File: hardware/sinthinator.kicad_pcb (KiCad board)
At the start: 2 copper layers, 100.9 x 144.5 mm, 56 parts, among them J1 3.5mm TRRS, J2 USB-C, M2 MountingHole_2.2mm_M2, SW1 SW_Push, SW2 SW_Push, SW3 SW_Push, U1 CAP1206, U2 PCA9544APW, U3 MCP4725, U4 CAP1206, U5 CAP1206, U7 AMS1117-3.3, U8 PAM8302A, U9 STM32C011F6

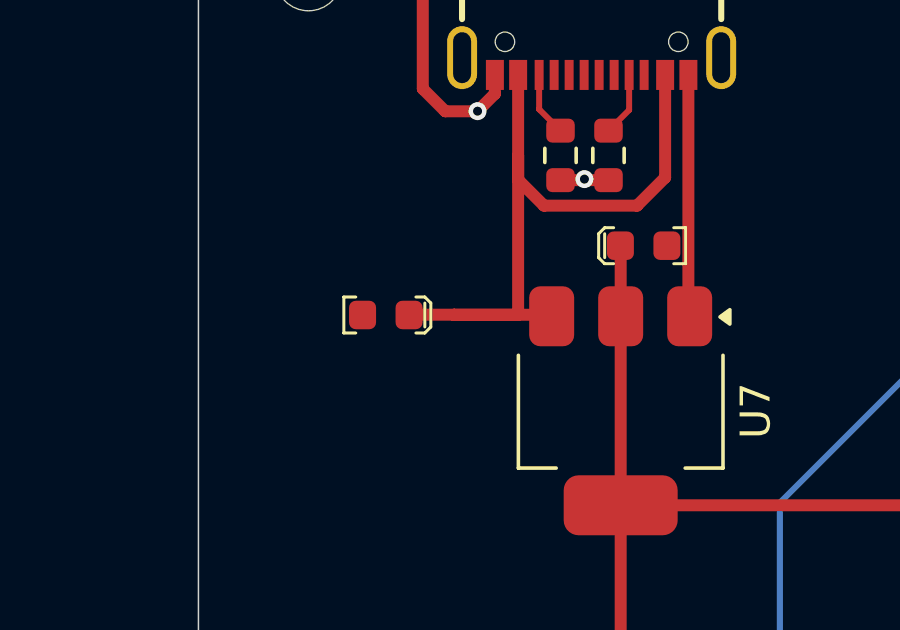
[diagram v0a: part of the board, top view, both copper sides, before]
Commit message: Ignore mount hole warnings + give them unique designators
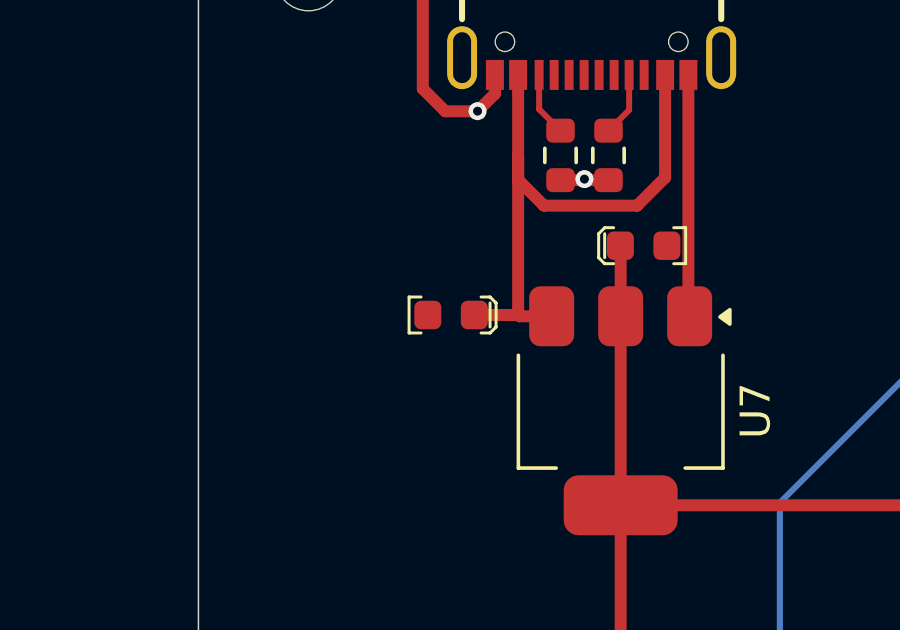
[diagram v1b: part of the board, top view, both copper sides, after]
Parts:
- moved C3 2.17 mm to (108.0, 34.3)
- renumbered M2 to M2-1, M2 to M2-2, M2 to M2-3, M2 to M2-4
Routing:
- net /+5V: track 24.8 -> 20.6 mm
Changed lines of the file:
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@@
 		(descr "Mounting Hole 2.2mm, M2, no annular, generated by kicad-footprint-generator mountinghole.py")
 		(tags "mountinghole M2")
-		(property "Reference" "M2"
+		(property "Reference" "M2-4"
 			(at 0 -3.15 0)
 			(layer "F.SilkS")
@@
 	(footprint "PCM_SparkFun-Capacitor:C_0603_1608Metric_Polar"
 		(layer "F.Cu")
-		(at 105.83 34.27 180)
+		(at 108.005 34.27 180)
 		(tags "SparkFun capacitor")
 		(property "Reference" "C3"
@@
 		(descr "Mounting Hole 2.2mm, M2, no annular, generated by kicad-footprint-generator mountinghole.py")
 		(tags "mountinghole M2")
-		(property "Reference" "M2"
+		(property "Reference" "M2-3"
 			(at 0 -3.15 0)
 			(layer "F.SilkS")
@@
 		(descr "Mounting Hole 2.2mm, M2, no annular, generated by kicad-footprint-generator mountinghole.py")
 		(tags "mountinghole M2")
-		(property "Reference" "M2"
+		(property "Reference" "M2-2"
 			(at 0 -3.15 0)
 			(layer "F.SilkS")
@@
 		(descr "Mounting Hole 2.2mm, M2, no annular, generated by kicad-footprint-generator mountinghole.py")
 		(tags "mountinghole M2")
-		(property "Reference" "M2"
+		(property "Reference" "M2-1"
 			(at 0 -3.15 0)
 			(layer "F.SilkS")
@@
 	)
 	(segment
-		(start 108.108455 34.262646)
-		(end 111.308455 34.262646)
-		(width 0.4)
-		(layer "F.Cu")
-		(net "/+5V")
-	)
-	(segment
-		(start 108.108455 34.262646)
-		(end 108.105809 34.26)
-		(width 0.4)
-		(layer "F.Cu")
-		(net "/+5V")
-	)
-	(segment
 		(start 110.240455 29.762735)
 		(end 111.10272 30.625)
@@
 	)
 	(segment
-		(start 108.105809 34.26)
-		(end 106.615 34.26)
-		(width 0.4)
-		(layer "F.Cu")
-		(net "/+5V")
-	)
-	(segment
 		(start 111.10272 30.625)
 		(end 114.205 30.625)
@@
 	)
 	(segment
-		(start 106.615 34.26)
-		(end 106.605 34.27)
+		(start 110.247809 34.27)
+		(end 108.78 34.27)
 		(width 0.4)
 		(layer "F.Cu")
@@
 	)
 	(segment
-		(start 110.240455 34.262646)
-		(end 108.108455 34.262646)
+		(start 110.290455 34.312646)
+		(end 110.240455 34.262646)
 		(width 0.4)
 		(layer "F.Cu")
@@
 	)
 	(segment
+		(start 111.358455 34.312646)
+		(end 110.290455 34.312646)
+		(width 0.4)
+		(layer "F.Cu")
+		(net "/+5V")
+	)
+	(segment
 		(start 110.240455 26.267646)
 		(end 110.240455 28.96)
@@
 	)
 	(segment
+		(start 110.247809 34.27)
+		(end 110.290455 34.312646)
+		(width 0.4)
+		(layer "F.Cu")
+		(net "/+5V")
+	)
+	(segment
 		(start 120.5875 154.625)
 		(end 120.5875 154.637774)
@@
 		(members "2c141160-73b0-467d-93fd-55eaec704715")
 	)
-	(group ""
-		(locked yes)
-		(members "2e6c6510-f0d7-413a-9635-cf8b48ca87db" "b7869b3a-c80d-4252-87af-6cf3c73b669c"
-			"bd7f29c9-1741-49cc-bb5e-e3a078f3b3de" "e1ebeba2-a45d-4aba-97f8-5b69e4acdc79"
-		)
-	)
 	(embedded_fonts no)

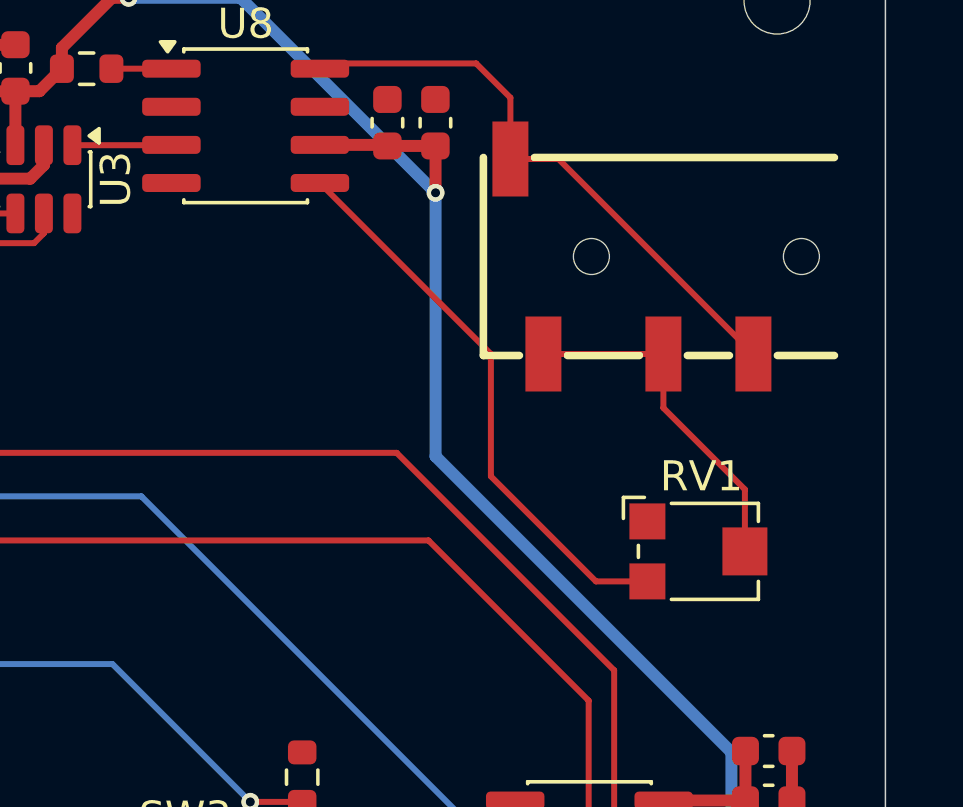
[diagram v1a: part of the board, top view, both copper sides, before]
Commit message: Add pads for audio output
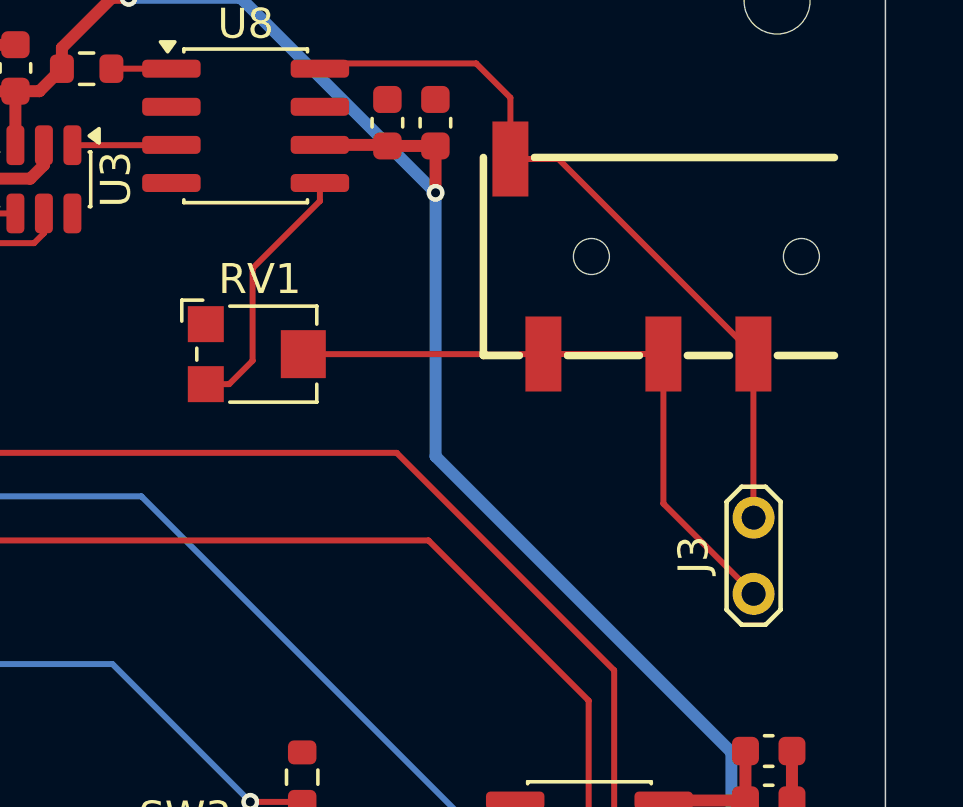
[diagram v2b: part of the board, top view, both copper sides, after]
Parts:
- added J3: Audio Out, TestPoint:TestPoint_2Pads_Pitch2.54mm_Drill0.8mm, F.Cu at (196.1, 42.8)
- moved RV1 16.1 mm to (179.6, 34.8)
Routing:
- net Net-(U8-OUT+): track 18.8 -> 8.74 mm
- net Net-(J3-Pin_1): track 11.7 -> 21.2 mm
- net Net-(J3-Pin_2): track 19.7 -> 25.2 mm
